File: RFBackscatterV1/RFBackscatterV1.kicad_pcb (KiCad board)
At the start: 2 copper layers, 3 parts, among them J1 SMA-J-P-H-RA-TH1, U1 SIT1534AI-H4-DCC-00.001E

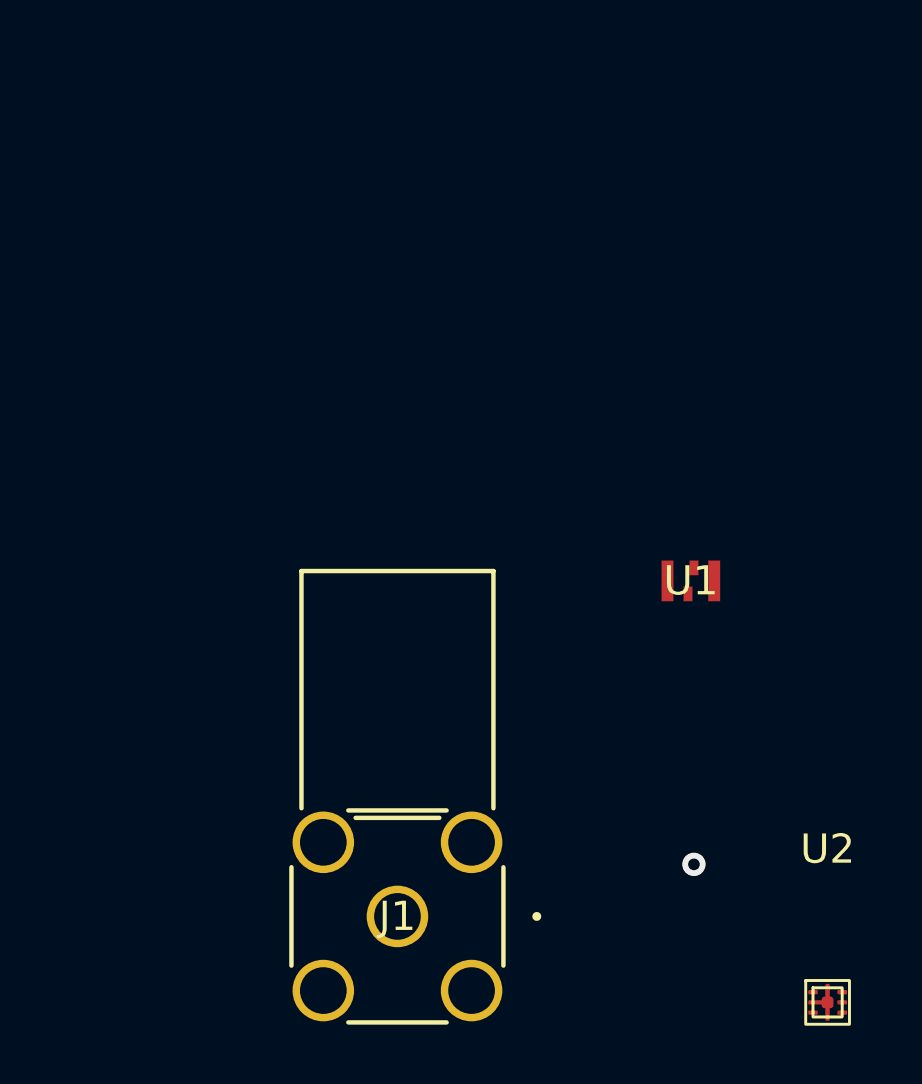
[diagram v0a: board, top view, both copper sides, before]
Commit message: updated board, added buffer and filter capacitors
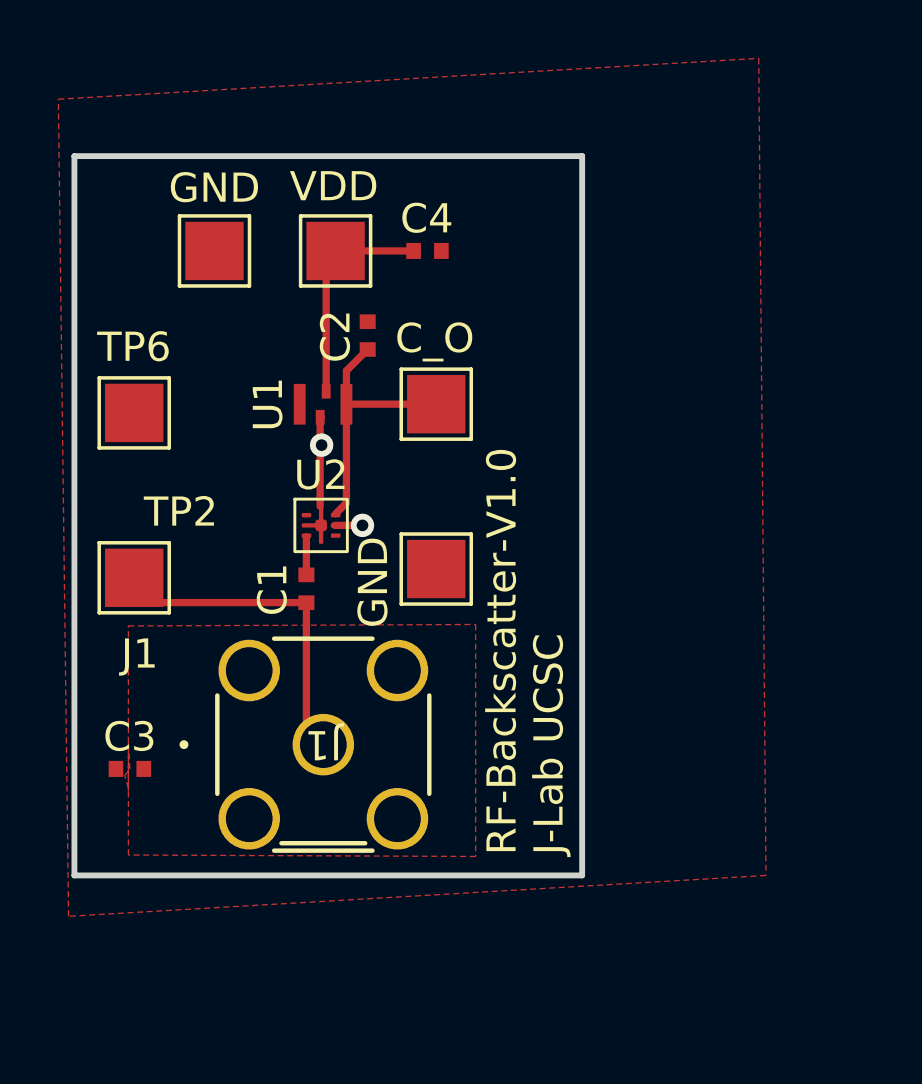
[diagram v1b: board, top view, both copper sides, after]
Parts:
- added C1: CBR04C101J3GAC, WADARfootprints:CAPC10555_55N_KEM, F.Cu at (169.6, 87.1)
- added C2: GJM1555C1H330JB01D, WADARfootprints:CAPC10555_55N_KEM, F.Cu at (171.7, 78.4)
- added C3: CBR04C101J3GAC, JLab_FP:CAPC10555_55N_KEM, F.Cu at (163.6, 93.2)
- added C4: GJM1555C1H330JB01D, WADARfootprints:CAPC10555_55N_KEM, F.Cu at (173.8, 75.5)
- added C_O: CLK_OUT, TestPoint:TestPoint_Pad_2.0x2.0mm, F.Cu at (174.1, 80.8)
- added GND: GND, TestPoint:TestPoint_Pad_2.0x2.0mm, F.Cu at (166.4, 75.5)
- added GND: GND, TestPoint:TestPoint_Pad_2.0x2.0mm, F.Cu at (174.1, 86.4)
- added TP2: OUTPUT2, TestPoint:TestPoint_Pad_2.0x2.0mm, F.Cu at (163.7, 86.7)
- added TP6: GND, TestPoint:TestPoint_Pad_2.0x2.0mm, F.Cu at (163.7, 81.0)
- added VDD: VDD, TestPoint:TestPoint_Pad_2.0x2.0mm, F.Cu at (170.6, 75.5)
- moved U2 23.8 mm to (170.1, 80.2)
- moved U1 14.0 mm to (170.2, 80.8)
- moved J1 6.41 mm to (170.2, 92.4), turned to 180 degrees
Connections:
- J1 pad 1: Net-(U2-OUTPUT2) -> Net-(C1-Pad2)
- J1 pad 2: GND -> RFGND
- J1 pad 3: GND -> RFGND
- J1 pad 4: GND -> RFGND
- J1 pad 5: GND -> RFGND
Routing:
- net Net-(C1-Pad2): track 0.00 -> 9.98 mm
- net Net-(U1-CLK_Out): track 0.00 -> 9.16 mm
- net +1V8: track 0.00 -> 7.61 mm, vias 1 -> 0
- net GND: track 0.00 -> 4.13 mm, vias 0 -> 2
- net Net-(U2-OUTPUT2): track 0.00 -> 1.30 mm
- added copper zone on F.Cu, net GND
- added copper zone on F.Cu, net RFGND
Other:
- board outline added: 17.4 x 24.7 mm
- board text added: "J1"
- board text added: "RF-Backscatter-V1.0 J-Lab UCSC"

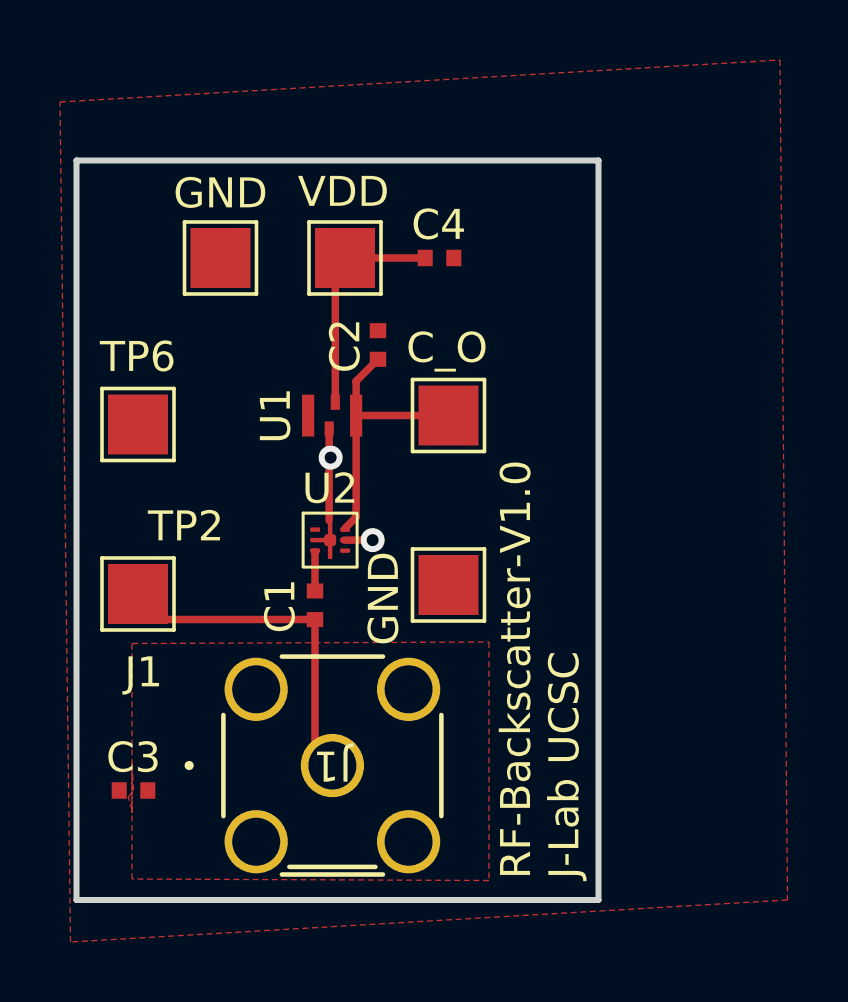
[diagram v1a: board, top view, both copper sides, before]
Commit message: generated manufacturing files for V1.0
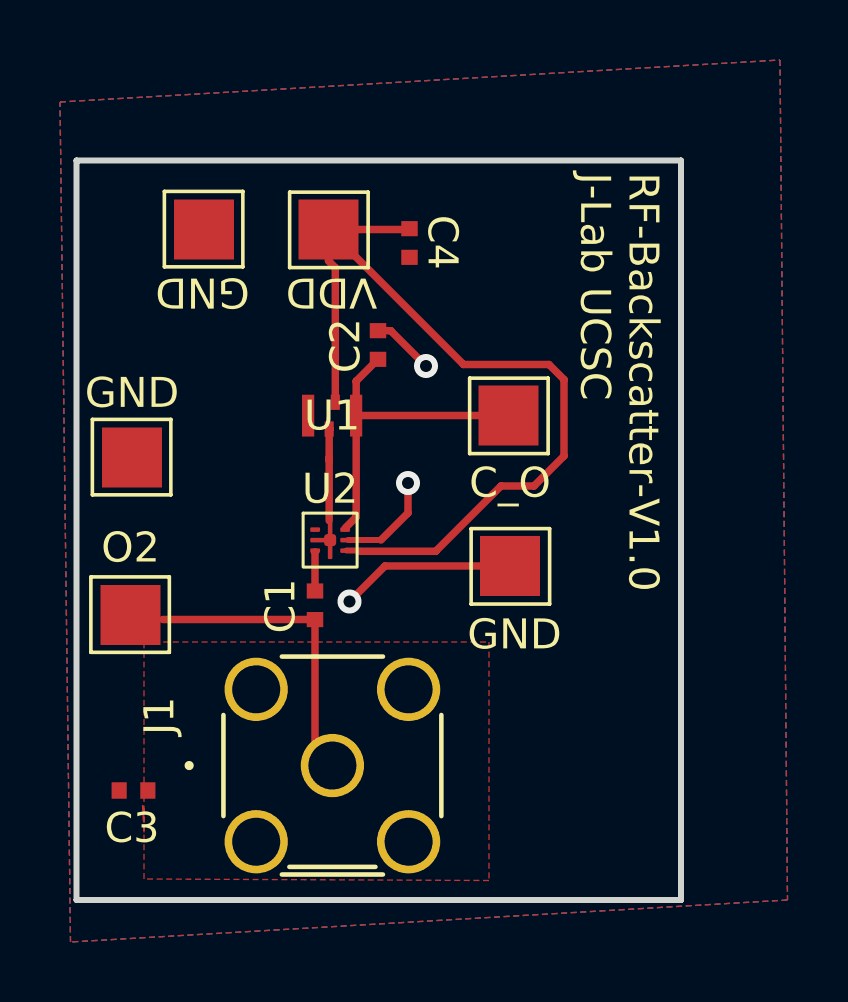
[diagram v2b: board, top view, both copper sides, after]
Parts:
- C_O, GND (x2), VDD: footprint TestPoint:TestPoint_Pad_2.0x2.0mm -> JLab_FP:EpicTestPointV1
- GND: renamed from TP6; footprint TestPoint:TestPoint_Pad_2.0x2.0mm -> JLab_FP:EpicTestPointV1
- O2: renamed from TP2; footprint TestPoint:TestPoint_Pad_2.0x2.0mm -> JLab_FP:EpicTestPointV1
- moved GND 3.83 mm to (165.4, 71.8), turned to 180 degrees
- moved C_O 3.68 mm to (176.5, 83.5)
- moved GND 3.28 mm to (176.6, 88.5)
- moved O2 2.16 mm to (163.0, 84.7), turned to 180 degrees
- moved VDD 1.80 mm to (170.5, 77.3)
- moved GND 1.77 mm to (163.0, 79.4), turned to 180 degrees
- moved C4 1.12 mm to (172.8, 75.0), turned to -90 degrees
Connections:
- net RFGND renamed Net-(C3-Pad2)
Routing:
- net +1V8: track 7.61 -> 29.6 mm
- net GND: track 4.13 -> 14.7 mm, vias 2 -> 3
- net Net-(U1-CLK_Out): track 9.16 -> 11.2 mm
- added copper zone on B.Cu, net GND
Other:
- board size 17.4 x 24.7 mm -> 20.2 x 24.7 mm

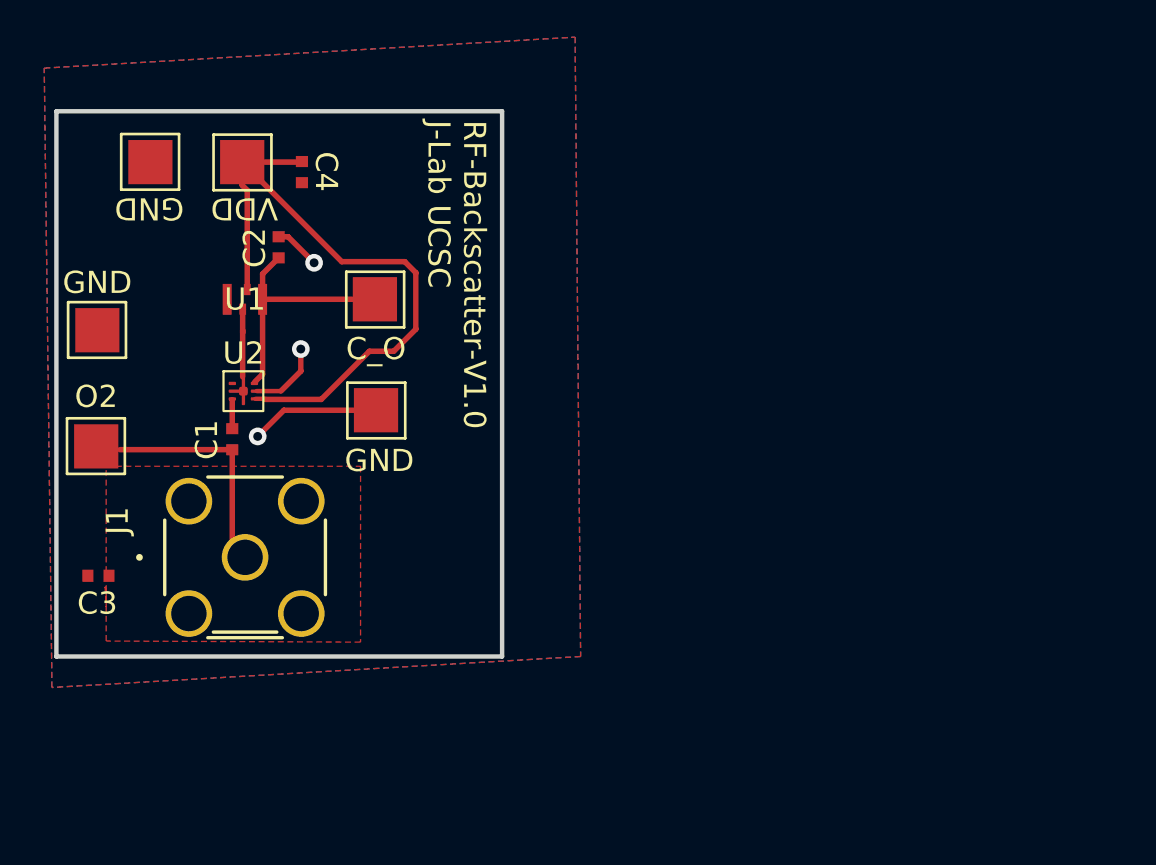
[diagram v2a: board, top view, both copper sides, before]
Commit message: fixed input pin capacitor and RF connector ground
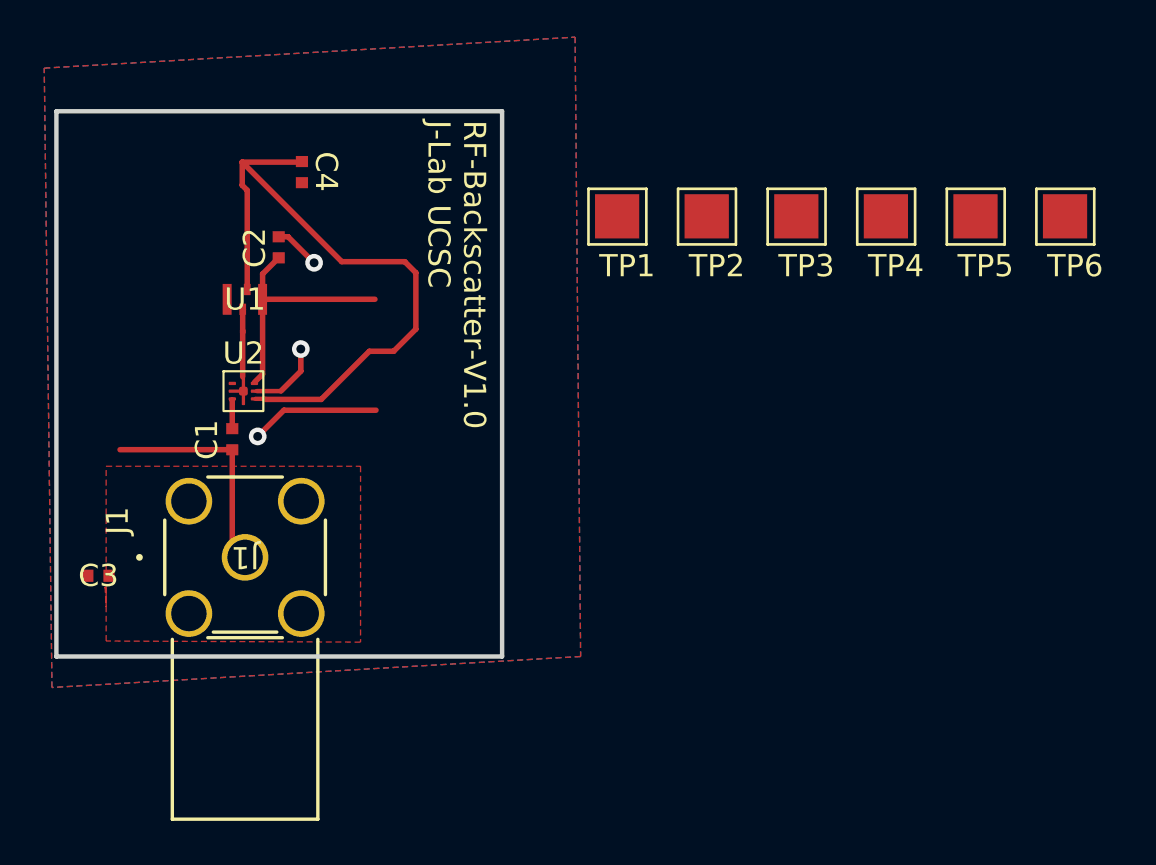
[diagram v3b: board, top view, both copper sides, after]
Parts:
- removed C_O: CLK_OUT, JLab_FP:EpicTestPointV1
- removed GND (x3): GND, JLab_FP:EpicTestPointV1
- removed O2: OUTPUT2, JLab_FP:EpicTestPointV1
- removed VDD: VDD, JLab_FP:EpicTestPointV1
- added TP1: VDD, JLab_FP:EpicTestPointV1, F.Cu at (187.5, 79.7)
- added TP2: OUTPUT2, JLab_FP:EpicTestPointV1, F.Cu at (191.5, 79.7)
- added TP3: CLK_OUT, JLab_FP:EpicTestPointV1, F.Cu at (195.6, 79.7)
- added TP4: GND, JLab_FP:EpicTestPointV1, F.Cu at (199.6, 79.7)
- added TP5: GND, JLab_FP:EpicTestPointV1, F.Cu at (203.7, 79.7)
- added TP6: GND, JLab_FP:EpicTestPointV1, F.Cu at (207.7, 79.7)
- C1, C3: value CBR04C101J3GAC -> 100pF
- C2, C4: value GJM1555C1H330JB01D -> 33pF
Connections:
- C3 pad 1: GND -> Net-(U2-INPUT)
- C3 pad 2: Net-(C3-Pad2) -> GND
- J1 pad 2: Net-(C3-Pad2) -> GND
- J1 pad 3: Net-(C3-Pad2) -> GND
- J1 pad 4: Net-(C3-Pad2) -> GND
- J1 pad 5: Net-(C3-Pad2) -> GND
- U2 pad 5: GND -> Net-(U2-INPUT)
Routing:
- net GND: track 14.7 -> 11.3 mm
- net Net-(U2-INPUT): track 0.00 -> 3.37 mm
- removed copper zone on F.Cu, net Net-(C3-Pad2)

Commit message: fixed design
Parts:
- moved TP6 42.8 mm to (165.0, 77.2)
- moved TP4 35.4 mm to (164.5, 84.2)
- moved TP2 28.3 mm to (164.5, 88.0)
- moved TP5 26.3 mm to (178.5, 87.2)
- moved TP1 19.2 mm to (168.5, 77.2)
- moved TP3 17.1 mm to (179.0, 83.7)
- moved C3 15.7 mm to (174.5, 82.0)
- moved C4 1.25 mm to (174.0, 75.0)
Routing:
- net +1V8: track 29.6 -> 41.4 mm
- net GND: track 11.3 -> 6.95 mm, vias 3 -> 2
- net Net-(U1-CLK_Out): track 11.2 -> 14.1 mm
- net Net-(U2-INPUT): track 3.37 -> 4.92 mm
- net Net-(C1-Pad2): track 9.98 -> 11.5 mm

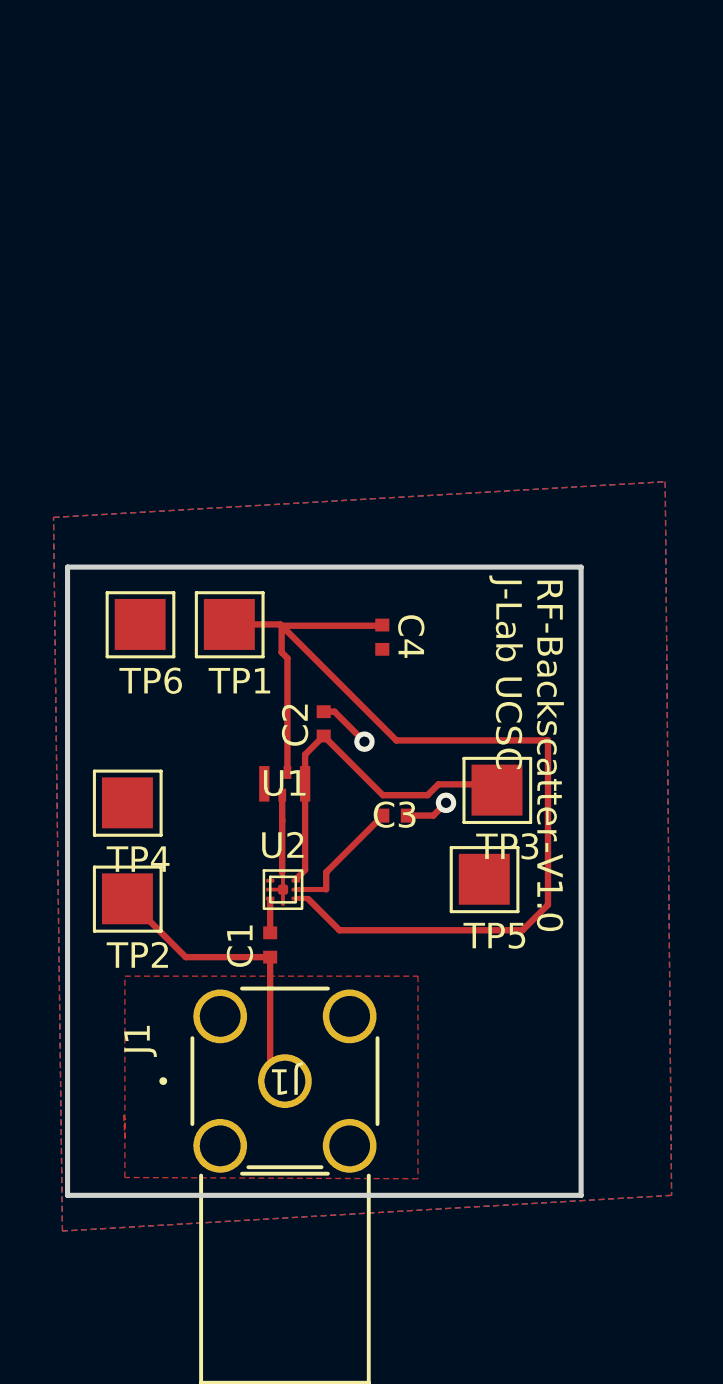
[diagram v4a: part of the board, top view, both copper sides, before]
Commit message: 1.1 added coin cell
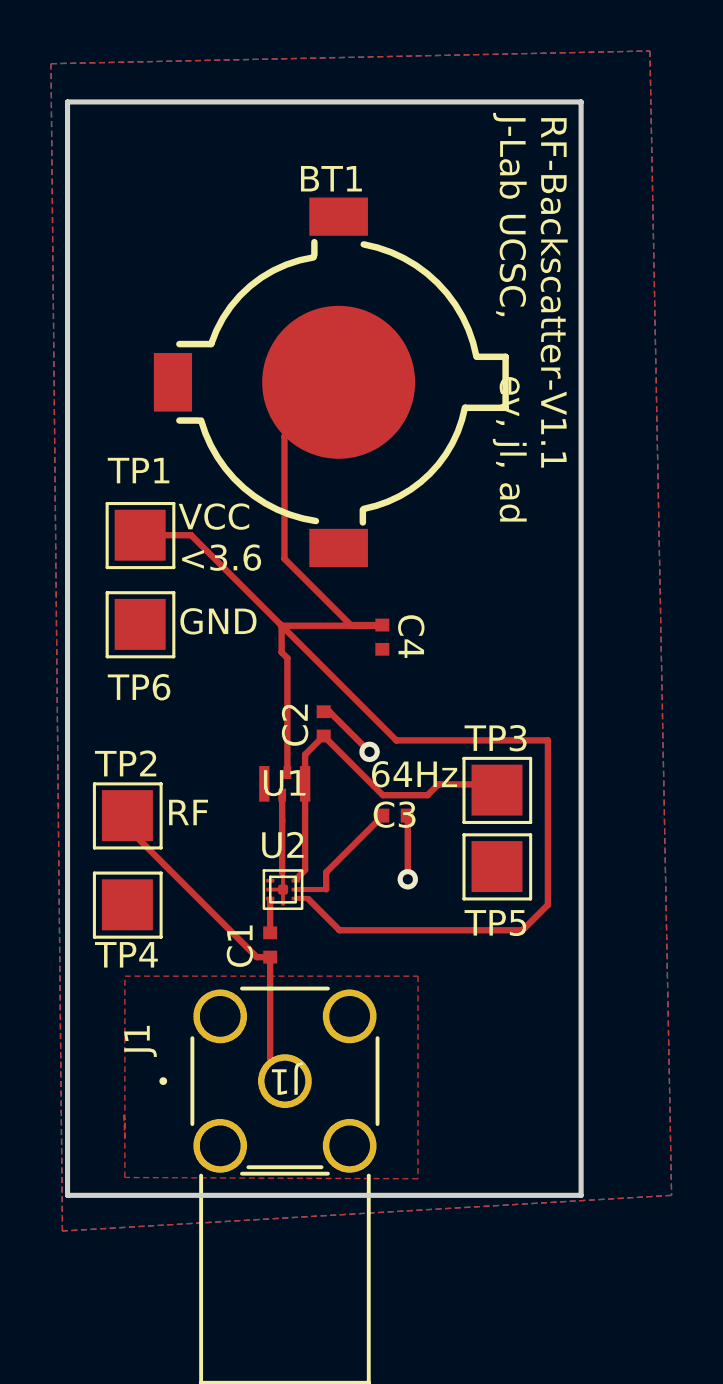
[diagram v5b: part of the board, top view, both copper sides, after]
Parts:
- removed TP1: VDD, JLab_FP:EpicTestPointV1
- added BT1: Battery_Cell, WADARfootprints:BAT-SMD_MY-LR44-02, F.Cu at (169.0, 65.0)
- added TP1 : VCC, JLab_FP:EpicTestPointV1, F.Cu at (165.0, 73.7)
- moved TP4 4.00 mm to (164.5, 88.2)
- moved TP2 3.27 mm to (164.5, 84.7)
- moved TP5 0.71 mm to (179.0, 86.7)
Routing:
- net +1V8: track 41.4 -> 59.2 mm
- net Net-(C1-Pad2): track 11.5 -> 13.6 mm
- net GND: track 6.95 -> 8.09 mm
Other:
- board size 20.2 x 24.7 mm -> 20.2 x 42.9 mm
- board text added: "64Hz"
- board text added: "GND"
- board text added: "RF"
- board text added: "RF-Backscatter-V1.1 J-Lab UCSC, ev, jl, ad"
- board text added: "VCC <3.6"
- board text removed: "RF-Backscatter-V1.0 J-Lab UCSC"

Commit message: PCB updated
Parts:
- removed C1: 100pF, WADARfootprints:CAPC10555_55N_KEM
- removed TP2: OUTPUT2, JLab_FP:EpicTestPointV1
- removed TP4: GND, JLab_FP:EpicTestPointV1
- added U3: 74LVC1GU04DRL, Package_TO_SOT_SMD:SOT-553, F.Cu at (169.0, 80.8)
- TP1: renamed from TP1 
- moved C4 6.25 mm to (171.5, 80.7)
- moved U1 4.36 mm to (167.6, 77.2)
- moved C3 2.32 mm to (172.7, 83.5)
- moved C2 2.03 mm to (170.2, 77.0)
- moved U2 1.51 mm to (170.0, 78.7)
- moved TP1 0.75 mm to (164.2, 73.7)
- moved TP6 0.75 mm to (164.2, 77.2)
- moved TP3 0.56 mm to (178.5, 83.5)
- moved TP5 0.50 mm to (178.5, 86.7)
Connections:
- C3 pad 2: GND -> Net-(C3-Pad2)
- C4 pad 1: +1V8 -> Net-(U2-VCTL2)
- J1 pad 1: Net-(C1-Pad2) -> Net-(C3-Pad2)
- U2 pad 1: unconnected-(U2-OUTPUT1-Pad1) -> GND
- U2 pad 3: Net-(U2-OUTPUT2) -> GND
- U2 pad 4: +1V8 -> Net-(U2-VCTL2)
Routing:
- net +1V8: track 59.2 -> 30.3 mm
- net Net-(U2-VCTL2): track 0.00 -> 19.0 mm, vias 0 -> 2
- net Net-(U1-CLK_Out): track 14.1 -> 30.1 mm, vias 0 -> 2
- net Net-(C1-Pad2): track 13.6 -> 0.00 mm
- net Net-(C3-Pad2): track 0.00 -> 10.6 mm
- net GND: track 8.09 -> 14.6 mm, vias 2 -> 8
- net Net-(U2-INPUT): track 4.92 -> 1.79 mm
- net Net-(U2-OUTPUT2): track 1.30 -> 0.00 mm
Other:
- board size 20.2 x 42.9 mm -> 19.3 x 42.2 mm
- board text added: "RF-Backscatter-V2.0 J-Lab UCSC ericdvet jlin"
- board text removed: "GND"
- board text removed: "RF"
- board text removed: "RF-Backscatter-V1.1 J-Lab UCSC, ev, jl, ad"
